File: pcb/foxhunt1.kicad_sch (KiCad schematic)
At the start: 0 parts

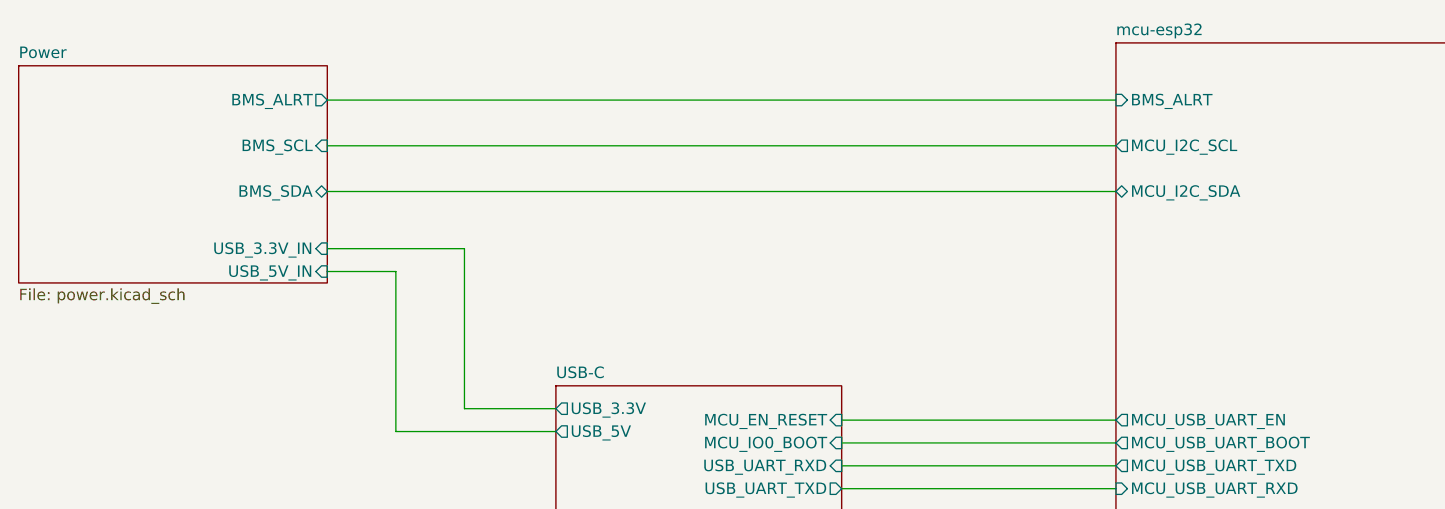
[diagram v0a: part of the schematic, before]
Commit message: Add TPS2121 Stage 2/3: USB-vs-battery priority muxing on 5V and 3.3V rails
power.kicad_sch:
- U14 (TPS2121RUXR): 5V rail mux. IN1=BATT_5V_REG (priority), IN2=USB_5V_IN,
  OUT=+5V. PR1 tied to IN1, CP2/OV1/OV2 to GND (VREF priority mode -- battery
  always wins when present, no voltage-comparison ambiguity between two
  nominally-5V sources). ILM set via R26 (30.1k, ~3.5A class, sized with
  margin above the 2A SA818 budget for TX current transients). SS via C42
  (0.01uF). ST feeds the battery/USB detect logic below.
- U13 (TPS2121RUXR): 3.3V rail mux, same configuration. IN1=BATT_3.3V_REG,
  IN2=USB_3.3V_IN, OUT=+3.3V. ILM via R25 (80.6k, ~1.5A class, vs 1A
  peripheral budget). SS via C41.
- U1 (74LVC1G08): AND-gates U13.ST and U14.ST (each pulled up individually
  via R27/R28, 10k to +3.3V, since ST is open-drain) into PWR_ON_BATTERY --
  high only when both rails are confirmed running from battery, low if
  either has fallen back to USB. Output exposed as a new Power sheet pin.

foxhunt1.kicad_sch: bridges PWR_ON_BATTERY (Power sheet) to the new
IO_IN_ON_BATT input on the mcu-esp32 sheet, and USB_3.3V_IN/USB_5V_IN
(Power sheet) to USB_3.3V/USB_5V (USB-C sheet) -- these were previously
unconnected placeholder labels.

mcu-esp32.kicad_sch: IO_IN_ON_BATT wired to U8 pin 35 (GPIO42), the one
GPIO the pinout doc had marked as still spare.

kicad_gx_library: TPS2121RUXR symbol fix (one OUT pin marked passive
instead of output, since the two physical OUT pins are meant to be tied
together -- avoids an ERC driver-conflict false positive).

power_regulation.kicad_sch, battery_18650_input.kicad_sch,
battery_powerpole_input.kicad_sch, foxhunt1.kicad_pro: incidental KiCad
save cleanup, no circuit changes (verified via orphan/short checks and
netlist diff -- same components as before).

Fully traced pin-by-pin: both mux dividers/ILM/SS wiring, the battery-vs-
USB source assignment on each rail (not swapped), the AND-gate inputs,
and all three cross-sheet bridges. 0 new orpha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
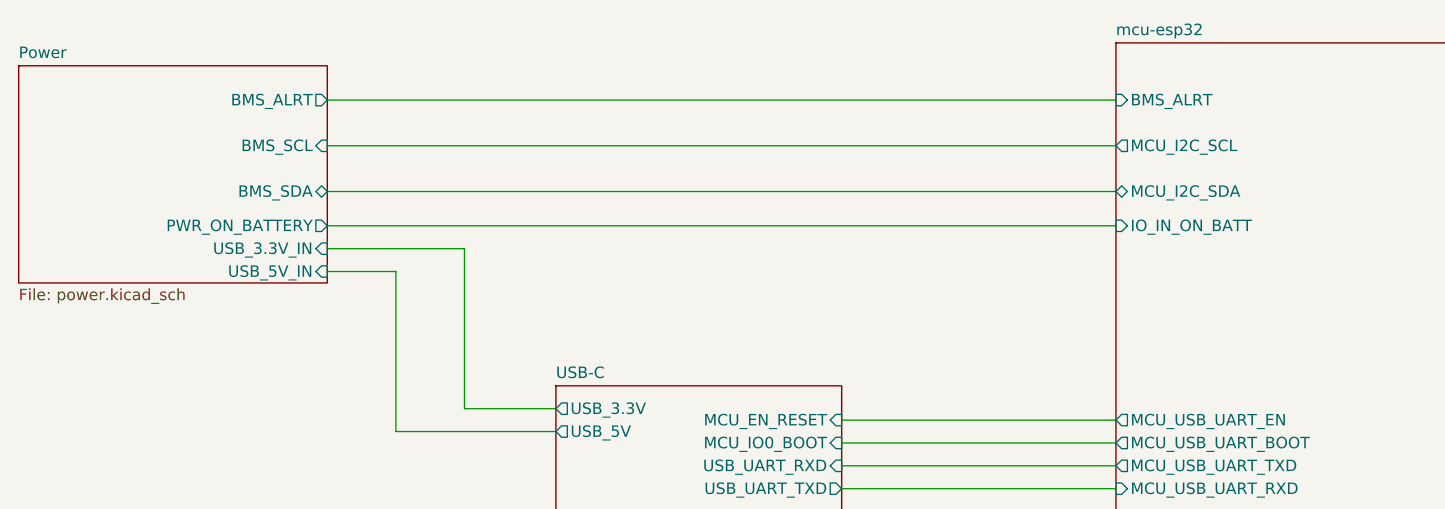
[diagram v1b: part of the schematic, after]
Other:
- sheet Power ports: added PWR_ON_BATTERY; removed none
- sheet mcu-esp32 ports: added IO_IN_ON_BATT; removed none
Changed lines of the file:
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@@
+	(wire
+		(pts
+			(xy 78.74 53.34) (xy 166.37 53.34)
+		)
+		(stroke
+			(width 0)
+			(type default)
+		)
+	)
 	(wire
 		(pts
@@
 			)
 		)
+		(pin "PWR_ON_BATTERY" output
+			(at 78.74 53.34 0)
+			(effects
+				(font
+					(size 1.27 1.27)
+				)
+				(justify right)
+			)
+		)
 		(instances
 			(project "foxhunt1"
@@
 			(effects
 				(font
+					(size 1.27 1.27)
+				)
+				(justify left)
+			)
+		)
+		(pin "IO_IN_ON_BATT" input
+			(at 166.37 53.34 180)
+			(effects
+				(font

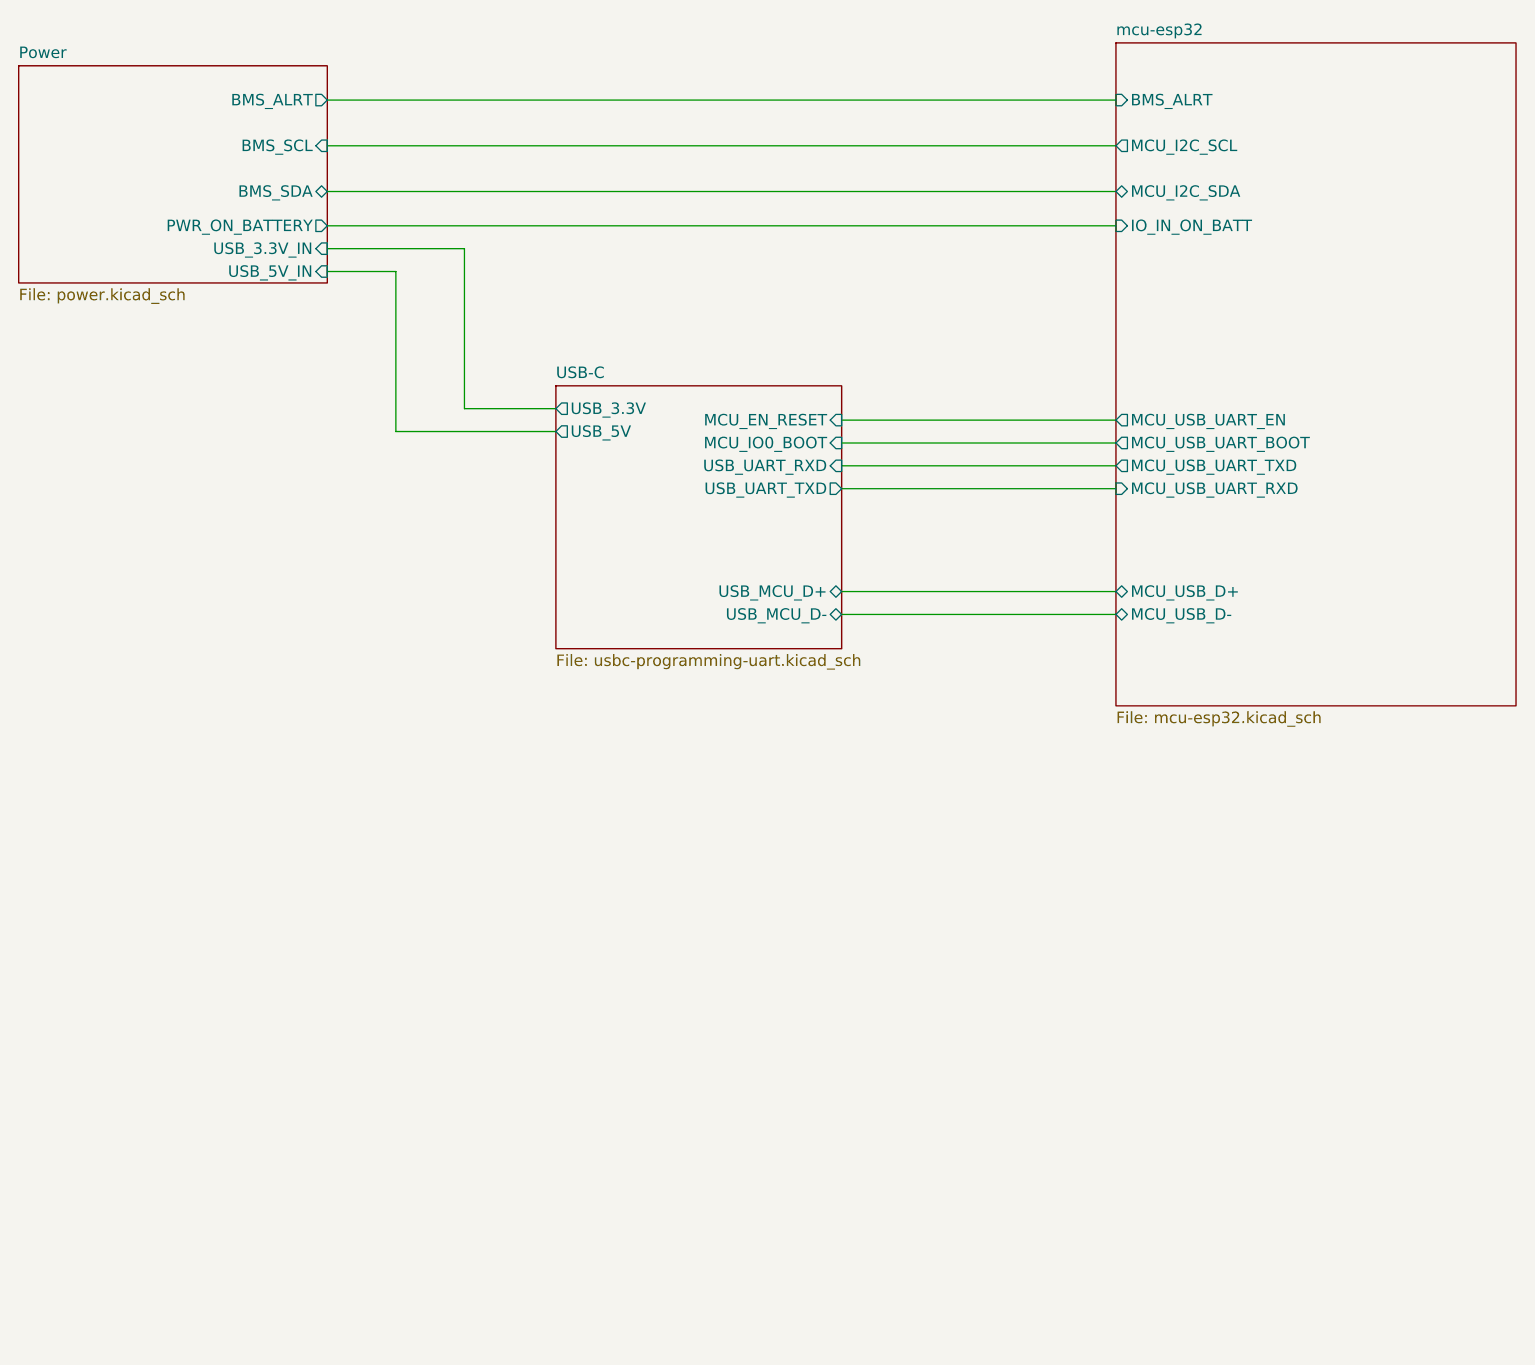
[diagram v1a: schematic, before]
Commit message: Add VRAW soft-latch power switch and MCU/RTC wake network
- Q5 (AO3407A P-FET) gates VRAW into Power Regulation, gate driven by
  a shared active-low wake node (button SW3, RTC_PWR_INTERRUPT,
  MCU_OUT_PWR_LATCH) pulled up to VRAW through 1M R29
- Q6 (BSS138) on the mcu-esp32 sheet lets GPIO48 hold the latch from
  a 3.3V-safe domain without exposing the MCU to VRAW voltage
- JP5/JP6 bench-isolation jumpers in the VRAW-gated path, bridged via
  new VRAW_GATED net label into Power Regulation's PWR_IN_SELECT
- JP24 lets USB be excluded from the TPS2121 power muxes for bench
  testing the sleep/wake cycle while still connected over USB-C
- Added blank Peripherals sheet (mcu-esp32 child) with RTC-facing
  pins stubbed and wired at the root, ready for the PCF8563 circuit
- regulation.md updated for the final 6.67V/4.78V intermediate
  voltages and matched-tolerance thin-film feedback dividers
- open_items.md: added power-off path as a follow-up (latch only
  handles power-on today)

Co-Authored-By: Claude Sonnet 5 <noreply@anthropic.com>
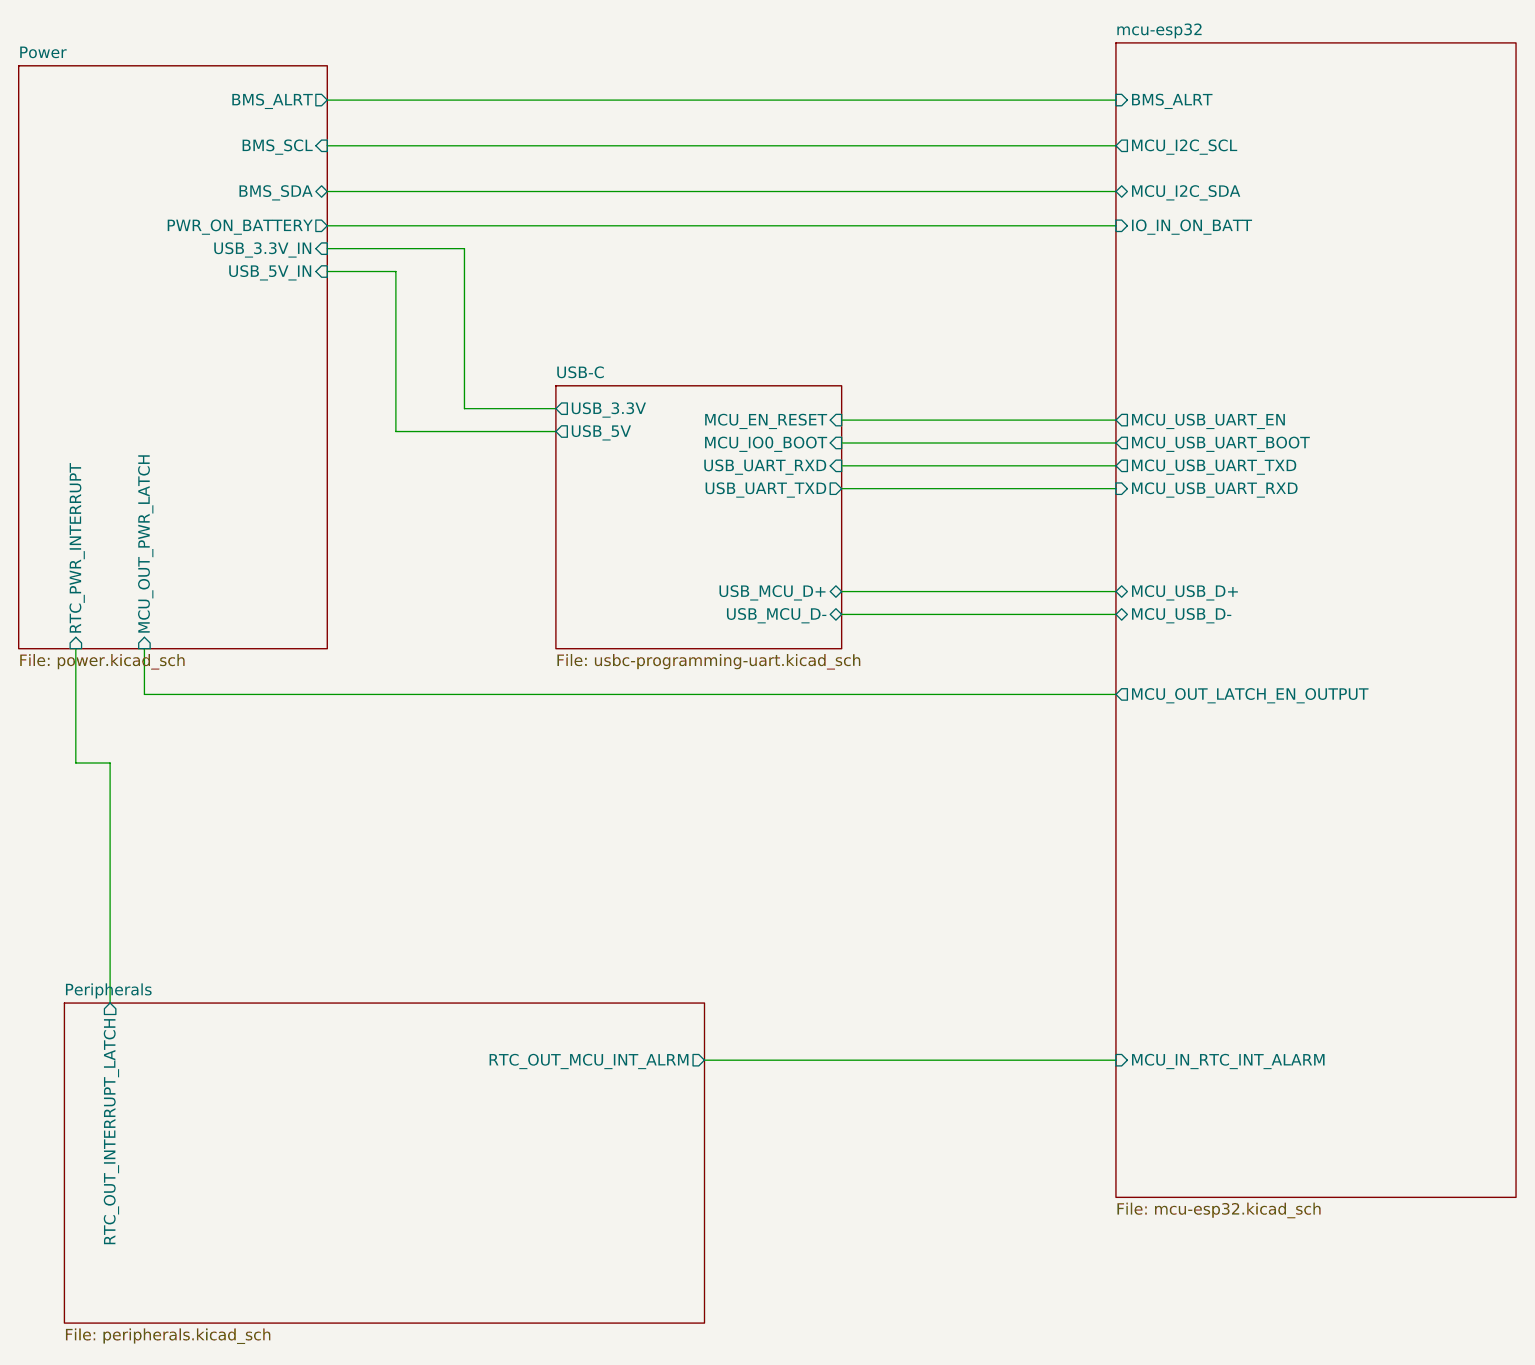
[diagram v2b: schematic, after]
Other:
- added sheet Peripherals (peripherals.kicad_sch)
- sheet Power ports: added MCU_OUT_PWR_LATCH, RTC_PWR_INTERRUPT; removed none
- sheet mcu-esp32 ports: added MCU_IN_RTC_INT_ALARM, MCU_OUT_LATCH_EN_OUTPUT; removed none
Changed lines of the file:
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@@
+	(wire
+		(pts
+			(xy 58.42 100.33) (xy 58.42 105.41)
+		)
+		(stroke
+			(width 0)
+			(type default)
+		)
+	)
 	(wire
 		(pts
@@
 	(wire
 		(pts
+			(xy 50.8 113.03) (xy 50.8 100.33)
+		)
+		(stroke
+			(width 0)
+			(type default)
+		)
+	)
+	(wire
+		(pts
+			(xy 54.61 113.03) (xy 50.8 113.03)
+		)
+		(stroke
+			(width 0)
+			(type default)
+		)
+	)
+	(wire
+		(pts
 			(xy 135.89 74.93) (xy 166.37 74.93)
 		)
@@
 		(pts
 			(xy 86.36 58.42) (xy 78.74 58.42)
+		)
+		(stroke
+			(width 0)
+			(type default)
+		)
+	)
+	(wire
+		(pts
+			(xy 58.42 105.41) (xy 166.37 105.41)
+		)
+		(stroke
+			(width 0)
+			(type default)
+		)
+	)
+	(wire
+		(pts
+			(xy 54.61 139.7) (xy 54.61 113.03)
+		)
+		(stroke
+			(width 0)
+			(type default)
+		)
+	)
+	(wire
+		(pts
+			(xy 120.65 146.05) (xy 166.37 146.05)
 		)
 		(stroke
@@
 	(sheet
 		(at 44.45 35.56)
-		(size 34.29 24.13)
+		(size 34.29 64.77)
 		(exclude_from_sim no)
 		(in_bom yes)
@@
 		)
 		(property "Sheetfile" "power.kicad_sch"
-			(at 44.45 60.2746 0)
+			(at 44.45 100.9146 0)
 			(show_name no)
 			(do_not_autoplace no)
@@
 				)
 				(justify right)
+			)
+		)
+		(pin "MCU_OUT_PWR_LATCH" input
+			(at 58.42 100.33 270)
+			(effects
+				(font
+					(size 1.27 1.27)
+				)
+				(justify left)
+			)
+		)
+		(pin "RTC_PWR_INTERRUPT" input
+			(at 50.8 100.33 270)
+			(effects
+				(font
+					(size 1.27 1.27)
+				)
+				(justify left)
 			)
 		)
@@
 	(sheet
 		(at 166.37 33.02)
-		(size 44.45 73.66)
+		(size 44.45 128.27)
 		(exclude_from_sim no)
 		(in_bom yes)
@@
 		)
 		(property "Sheetfile" "mcu-esp32.kicad_sch"
-			(at 166.37 107.2646 0)
+			(at 166.37 161.8746 0)
 			(show_name no)
 			(do_not_autoplace no)
@@
 		(pin "IO_IN_ON_BATT" input
 			(at 166.37 53.34 180)
+			(effects
+				(font
+					(size 1.27 1.27)
+				)
+				(justify left)
+			)
+		)
+		(pin "MCU_IN_RTC_INT_ALARM" input
+			(at 166.37 146.05 180)
+			(effects
+				(font
+					(size 1.27 1.27)
+				)
+				(justify left)
+			)
+		)
+		(pin "MCU_OUT_LATCH_EN_OUTPUT" output
+			(at 166.37 105.41 180)
 			(effects
 				(font
@@
 				)
 			)
+		)
+	)
+	(sheet
+		(at 49.53 139.7)
+		(size 71.12 35.56)
+		(exclude_from_sim no)
+		(in_bom yes)
+		(on_board yes)
+		(dnp no)
+		(fields_autoplaced yes)
+		(stroke
+			(width 0.1524)
+			(type solid)
+		)
+		(fill
+			(color 0 0 0 0)
+		)
+		(property "Sheetname" "Peripherals"
+			(at 49.53 138.9884 0)
+			(show_name no)
+			(do_not_autoplace no)
+			(effects
+				(font
+					(size 1.27 1.27)
+				)
+				(justify left bottom)
+			)
+		)
+		(property "Sheetfile" "peripherals.kicad_sch"
+			(at 49.53 175.8446 0)
+			(show_name no)
+			(do_not_autoplace no)
+			(effects
+				(font
+					(size 1.27 1.27)
+				)
+				(justify left top)
+			)
+		)
+		(pin "RTC_OUT_INTERRUPT_LATCH" output
+			(at 54.61 139.7 90)
+			(effects
+				(font
+					(size 1.27 1.27)
+				)
+				(justify right)
+			)
+		)
+		(pin "RTC_OUT_MCU_INT_ALRM" output
+			(at 120.65 146.05 0)
+			(effects
+				(font
+					(size 1.27 1.27)
+				)
+				(justify right)
+			)
+		)
+		(instances
+			(project "foxhunt1"
+				(path "/8399ba4b-9428-480d-8b65-76cf154b97a5"
+					(page "8")
+				)
+			)
